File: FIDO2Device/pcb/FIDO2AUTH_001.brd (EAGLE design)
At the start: 22.9 x 34.9 mm, 25 parts, among them CN1 TE-1734028, SW1 SKRPACE010, SW2 SKTADAE010, U1 MDBT50Q-P1M, X1 NX3215SA-32.768K

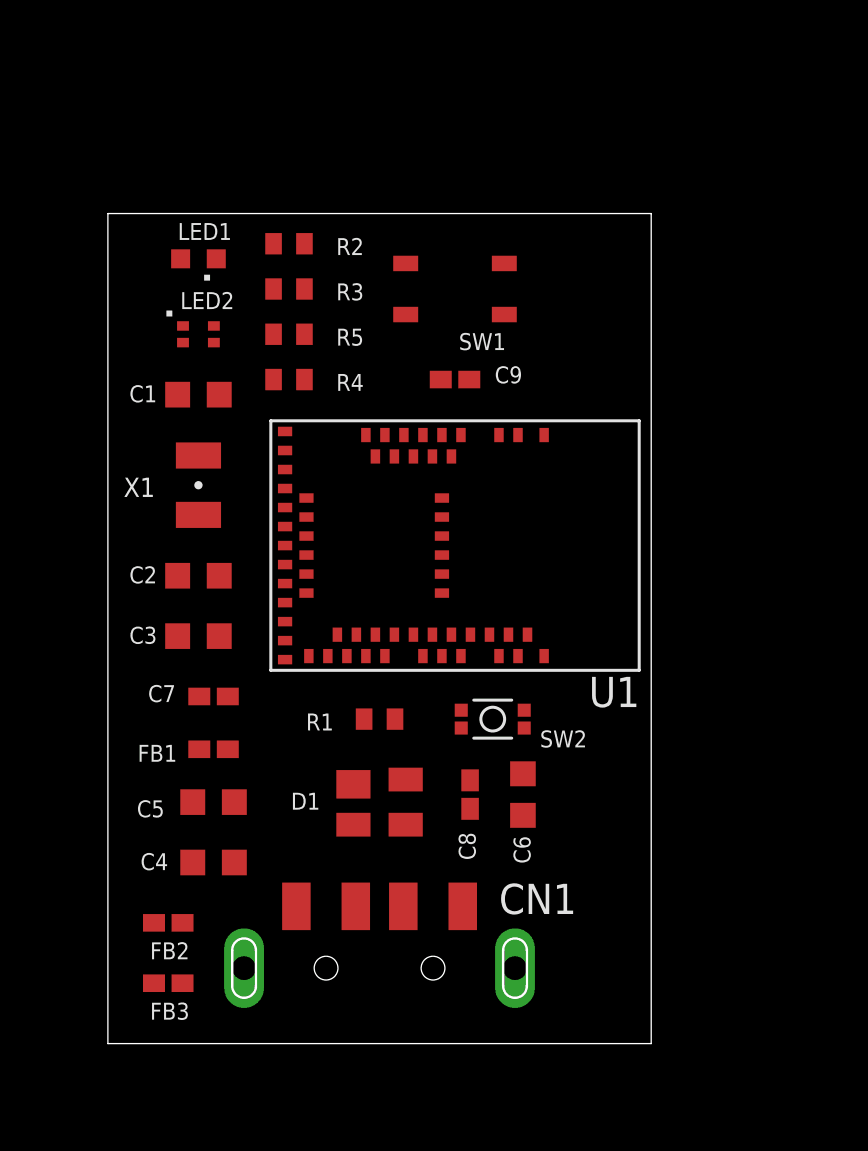
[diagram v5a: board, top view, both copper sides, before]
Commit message: [WIP] ブレークアウト基板回路図
・プログラミング・インターフェース（5Pスルーホール）配置
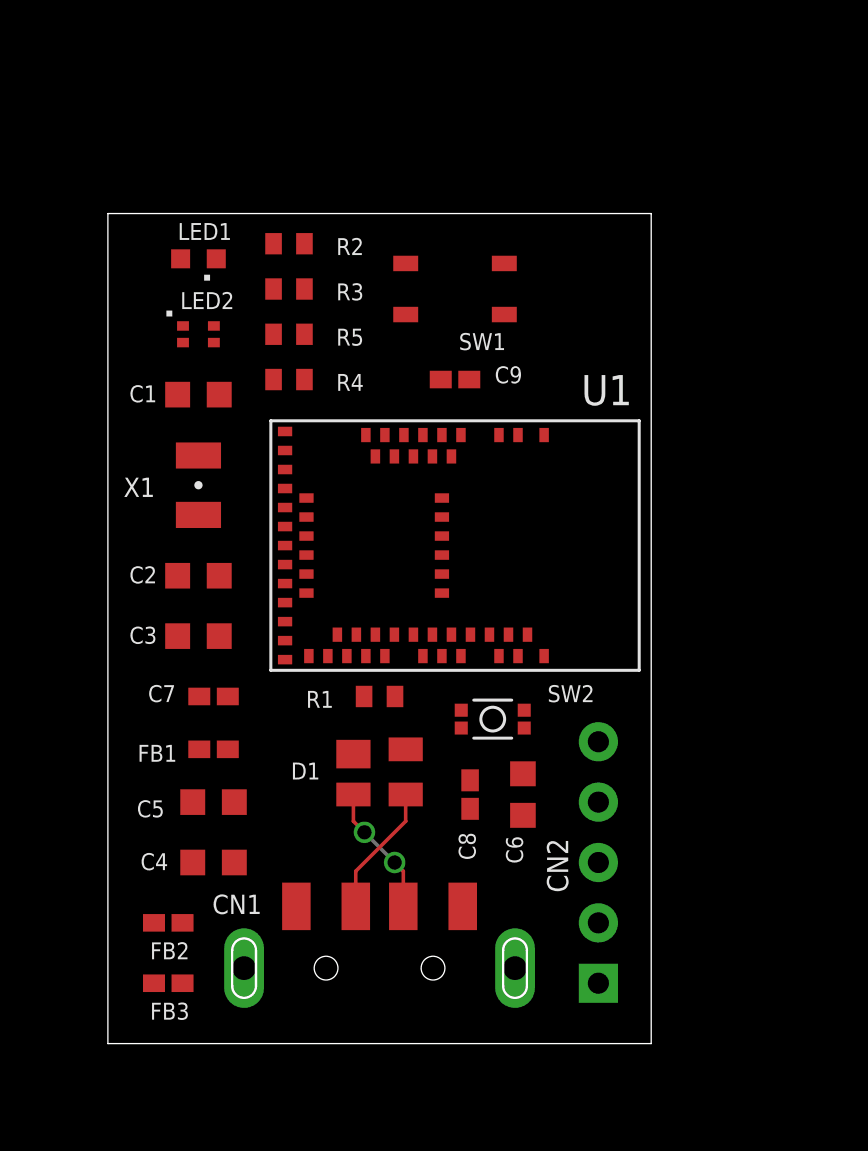
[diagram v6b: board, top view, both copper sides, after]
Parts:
- added CN2: IF_5PIN_H, Connectors:HEADER_5PIN
- moved D1 1.27 mm to (11.4, 11.4)
- moved R1 0.95 mm to (11.4, 14.6)
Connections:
- net 0V: now also CN2.1
- net RESET: now also CN2.5
- net SWDCLK: now also CN2.3
- net SWDIO: now also CN2.2
- net VDD_NRF: now also CN2.4
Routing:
- net D_P: track 0.00 -> 5.57 mm
- net D_N: track 0.00 -> 5.57 mm, vias 0 -> 2
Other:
- board text added: "GND"
- board text added: "PCLK"
- board text added: "PIO"
- board text added: "RST"
- board text added: "VDD"
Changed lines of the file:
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@@
 <wire x1="22.86" y1="34.925" x2="0" y2="34.925" width="0" layer="20"/>
 <wire x1="0" y1="34.925" x2="0" y2="0" width="0" layer="20"/>
+<text x="21.9075" y="2.54" size="0.6096" layer="22" rot="R90" align="top-center">GND</text>
+<text x="21.9075" y="10.16" size="0.6096" layer="22" rot="R90" align="top-center">VDD</text>
+<text x="21.9075" y="12.7" size="0.6096" layer="22" rot="R90" align="top-center">RST</text>
+<text x="21.9075" y="7.62" size="0.6096" layer="22" rot="R90" align="top-center">PCLK</text>
+<text x="21.9075" y="5.08" size="0.6096" layer="22" rot="R90" align="top-center">PIO</text>
 </plain>
 <attributes>
@@
 <elements>
 <element name="U1" library="Parts" package="MDBT50Q-P1M" value="MDBT50Q-P1M" x="14.605" y="20.955" smashed="yes" rot="R270">
-<attribute name="NAME" x="20.235" y="14.16" size="1.27" layer="25"/>
+<attribute name="NAME" x="19.9175" y="26.86" size="1.27" layer="25"/>
 <attribute name="VALUE" x="6.475" y="26.225" size="1.27" layer="27" rot="R270" align="top-left"/>
 </element>
@@
 </element>
 <element name="C6" library="Parts" package="C0603K" value="10uF" x="17.4625" y="10.4775" smashed="yes" rot="R270">
-<attribute name="NAME" x="17.071975" y="8.7376" size="0.7112" layer="25" rot="R270"/>
+<attribute name="NAME" x="16.754475" y="8.7376" size="0.7112" layer="25" rot="R270"/>
 <attribute name="VALUE" x="15.97125" y="11.2775" size="0.7112" layer="27" rot="R270"/>
 </element>
@@
 <attribute name="VALUE" x="3.913125" y="3.99" size="0.7112" layer="27" rot="R180"/>
 </element>
-<element name="D1" library="Parts" package="SOT143B" value="PRTR5V0U2X" x="11.43" y="10.16" smashed="yes" rot="R270">
-<attribute name="NAME" x="7.699375" y="9.8425" size="0.7112" layer="25"/>
-<attribute name="VALUE" x="8.41375" y="11.58875" size="0.7112" layer="27" rot="R270"/>
+<element name="D1" library="Parts" package="SOT143B" value="PRTR5V0U2X" x="11.43" y="11.43" smashed="yes" rot="R270">
+<attribute name="NAME" x="7.699375" y="11.1125" size="0.7112" layer="25"/>
+<attribute name="VALUE" x="8.41375" y="12.85875" size="0.7112" layer="27" rot="R270"/>
 </element>
 <element name="CN1" library="Connectors" package="TE-1734028" value="TE-1734028" x="11.43" y="3.175" smashed="yes">
-<attribute name="NAME" x="16.455" y="5.4525" size="1.27" layer="25"/>
+<attribute name="NAME" x="4.39" y="5.4525" size="0.8128" layer="25"/>
 <attribute name="VALUE" x="6.93" y="-1.325" size="1.27" layer="27"/>
 </element>
-<element name="R1" library="Parts" package="R0402" value="10k" x="11.43" y="13.6525" smashed="yes">
-<attribute name="NAME" x="8.334375" y="13.17625" size="0.7112" layer="25"/>
-<attribute name="VALUE" x="10.874375" y="12.22375" size="0.7112" layer="27"/>
+<element name="R1" library="Parts" package="R0402" value="10k" x="11.43" y="14.605" smashed="yes">
+<attribute name="NAME" x="8.334375" y="14.12875" size="0.7112" layer="25"/>
+<attribute name="VALUE" x="10.874375" y="13.17625" size="0.7112" layer="27"/>
 </element>
 <element name="C9" library="Parts" package="C0402K" value="0.1uF" x="14.605" y="27.94" smashed="yes">
@@
 <element name="SW1" library="Parts" package="SKRPACE010" value="SKRPACE010" x="14.605" y="31.75" rot="R180"/>
 <element name="SW2" library="Parts" package="SKTADAE010" value="SKTADAE010" x="16.1925" y="13.6525" smashed="yes" rot="R180">
-<attribute name="NAME" x="18.176875" y="12.461875" size="0.7112" layer="25" ratio="11"/>
+<attribute name="NAME" x="18.494375" y="14.366875" size="0.7112" layer="25" ratio="11"/>
 <attribute name="VALUE" x="17.541875" y="14.938375" size="0.7112" layer="27" ratio="11" rot="R180" align="top-left"/>
 </element>
@@
 <attribute name="NAME" x="9.604375" y="29.36875" size="0.7112" layer="25"/>
 <attribute name="VALUE" x="7.064375" y="28.41625" size="0.7112" layer="27"/>
+</element>
+<element name="CN2" library="Connectors" package="HEADER_5PIN" value="IF_5PIN_H" x="20.6375" y="2.54" smashed="yes" rot="R90">
+<attribute name="NAME" x="19.3675" y="6.35" size="0.889" layer="25" ratio="11" rot="R90"/>
+<attribute name="VALUE" x="21.9075" y="1.27" size="0.889" layer="27" ratio="11" rot="R90" align="top-left"/>
 </element>
 </elements>
@@
 <contactref element="SW2" pad="3"/>
 <contactref element="SW2" pad="1"/>
+<contactref element="CN2" pad="1"/>
 <wire x1="12.53" y1="32.825" x2="16.68" y2="32.825" width="0" layer="19" extent="1-1"/>
-<wire x1="15.205" y1="27.94" x2="12.53" y2="32.825" width="0" layer="19" extent="1-1"/>
+<wire x1="15.205" y1="27.94" x2="16.68" y2="32.825" width="0" layer="19" extent="1-1"/>
 <wire x1="17.255" y1="25.605" x2="15.205" y2="27.94" width="0" layer="19" extent="1-1"/>
 <wire x1="18.355" y1="25.605" x2="17.255" y2="25.605" width="0" layer="19" extent="1-1"/>
@@
 <wire x1="1.94" y1="5.08" x2="3.57" y2="7.62" width="0" layer="19" extent="1-1"/>
 <wire x1="1.94" y1="2.54" x2="1.94" y2="5.08" width="0" layer="19" extent="1-1"/>
-<wire x1="10.33" y1="10.91" x2="7.455" y2="16.155" width="0" layer="19" extent="1-1"/>
-<wire x1="15.24" y1="9.8775" x2="10.33" y2="10.91" width="0" layer="19" extent="1-1"/>
+<wire x1="10.33" y1="12.18" x2="7.455" y2="16.155" width="0" layer="19" extent="1-1"/>
+<wire x1="15.24" y1="9.8775" x2="10.33" y2="12.18" width="0" layer="19" extent="1-1"/>
 <wire x1="17.4625" y1="9.6025" x2="15.24" y2="9.8775" width="0" layer="19" extent="1-1"/>
 <wire x1="17.5175" y1="13.2775" x2="17.4625" y2="9.6025" width="0" layer="19" extent="1-1"/>
 <wire x1="17.5175" y1="14.0275" x2="17.5175" y2="13.2775" width="0" layer="19" extent="1-1"/>
 <wire x1="18.355" y1="16.305" x2="17.5175" y2="14.0275" width="0" layer="19" extent="1-1"/>
+<wire x1="20.6375" y1="2.54" x2="17.4625" y2="9.6025" width="0" layer="19" extent="1-1"/>
 </signal>
 <signal name="XL1">
@@
 <signal name="SWDCLK">
 <contactref element="U1" pad="53"/>
+<contactref element="CN2" pad="3"/>
+<wire x1="20.6375" y1="7.62" x2="17.255" y2="16.305" width="0" layer="19" extent="1-1"/>
 </signal>
 <signal name="SWDIO">
 <contactref element="U1" pad="51"/>
+<contactref element="CN2" pad="2"/>
+<wire x1="20.6375" y1="5.08" x2="16.455" y2="16.305" width="0" layer="19" extent="1-1"/>
 </signal>
 <signal name="RESET">
@@
 <contactref element="SW2" pad="2"/>
 <contactref element="SW2" pad="4"/>
+<contactref element="CN2" pad="5"/>
 <wire x1="11.255" y1="17.205" x2="14.005" y2="27.94" width="0" layer="19" extent="1-1"/>
-<wire x1="12.08" y1="13.6525" x2="11.255" y2="17.205" width="0" layer="19" extent="1-1"/>
-<wire x1="14.8675" y1="13.2775" x2="12.08" y2="13.6525" width="0" layer="19" extent="1-1"/>
-<wire x1="14.8675" y1="14.0275" x2="14.8675" y2="13.2775" width="0" layer="19" extent="1-1"/>
+<wire x1="12.08" y1="14.605" x2="11.255" y2="17.205" width="0" layer="19" extent="1-1"/>
+<wire x1="14.8675" y1="14.0275" x2="12.08" y2="14.605" width="0" layer="19" extent="1-1"/>
+<wire x1="14.8675" y1="13.2775" x2="14.8675" y2="14.0275" width="0" layer="19" extent="1-1"/>
+<wire x1="20.6375" y1="12.7" x2="14.8675" y2="13.2775" width="0" layer="19" extent="1-1"/>
 </signal>
 <signal name="D_P">
@@
 <contactref element="D1" pad="3"/>
 <contactref element="CN1" pad="3"/>
-<wire x1="12.53" y1="9.21" x2="9.255" y2="16.305" width="0" layer="19" extent="1-1"/>
-<wire x1="10.43" y1="5.775" x2="12.53" y2="9.21" width="0" layer="19" extent="1-1"/>
+<wire x1="10.43" y1="5.775" x2="10.43" y2="7.255" width="0.1524" layer="1"/>
+<wire x1="12.53" y1="10.48" x2="12.53" y2="9.355" width="0.1524" layer="1"/>
+<wire x1="12.53" y1="9.355" x2="10.43" y2="7.255" width="0.1524" layer="1"/>
+<wire x1="12.53" y1="10.48" x2="9.255" y2="16.305" width="0" layer="19" extent="1-1"/>
 </signal>
 <signal name="D_N">
@@
 <contactref element="D1" pad="2"/>
 <contactref element="CN1" pad="2"/>
-<wire x1="10.33" y1="9.21" x2="8.455" y2="16.305" width="0" layer="19" extent="1-1"/>
-<wire x1="12.43" y1="5.775" x2="10.33" y2="9.21" width="0" layer="19" extent="1-1"/>
+<via x="10.795" y="8.89" extent="1-16" drill="0.6"/>
+<via x="12.065" y="7.62" extent="1-16" drill="0.6"/>
+<wire x1="12.43" y1="5.775" x2="12.43" y2="7.255" width="0.1524" layer="1"/>
+<wire x1="12.43" y1="7.255" x2="12.065" y2="7.62" width="0.1524" layer="1"/>
+<wire x1="10.795" y1="8.89" x2="10.33" y2="9.355" width="0.1524" layer="1"/>
+<wire x1="10.33" y1="9.355" x2="10.33" y2="10.48" width="0.1524" layer="1"/>
+<wire x1="10.795" y1="8.89" x2="12.065" y2="7.62" width="0.1524" layer="16"/>
+<wire x1="10.33" y1="10.48" x2="8.455" y2="16.305" width="0" layer="19" extent="1-1"/>
 </signal>
 <signal name="VDD_NRF">
@@
 <contactref element="LED1" pad="A"/>
 <contactref element="LED2" pad="1"/>
+<contactref element="CN2" pad="4"/>
 <wire x1="3.16" y1="30.195" x2="3.06" y2="33.02" width="0" layer="19" extent="1-1"/>
 <wire x1="7.455" y1="19.355" x2="3.16" y2="30.195" width="0" layer="19" extent="1-1"/>
 <wire x1="7.455" y1="18.555" x2="7.455" y2="19.355" width="0" layer="19" extent="1-1"/>
 <wire x1="4.685" y1="17.145" x2="7.455" y2="18.555" width="0" layer="19" extent="1-1"/>
-<wire x1="10.78" y1="13.6525" x2="7.455" y2="18.555" width="0" layer="19" extent="1-1"/>
+<wire x1="10.78" y1="14.605" x2="7.455" y2="18.555" width="0" layer="19" extent="1-1"/>
+<wire x1="20.6375" y1="10.16" x2="10.78" y2="14.605" width="0" layer="19" extent="1-1"/>
 </signal>
 <signal name="VBUS">
@@
 <contactref element="D1" pad="4"/>
 <wire x1="17.4625" y1="11.3525" x2="15.24" y2="11.0775" width="0" layer="19" extent="1-1"/>
-<wire x1="12.53" y1="11.11" x2="15.24" y2="11.0775" width="0" layer="19" extent="1-1"/>
+<wire x1="12.53" y1="12.38" x2="15.24" y2="11.0775" width="0" layer="19" extent="1-1"/>
 <wire x1="14.93" y1="5.775" x2="15.24" y2="11.0775" width="0" layer="19" extent="1-1"/>
-<wire x1="5.32" y1="10.16" x2="12.53" y2="11.11" width="0" layer="19" extent="1-1"/>
+<wire x1="5.32" y1="10.16" x2="12.53" y2="12.38" width="0" layer="19" extent="1-1"/>
 <wire x1="3.845" y1="12.3825" x2="5.32" y2="10.16" width="0" layer="19" extent="1-1"/>
 </signal>

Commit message: [WIP] ブレークアウト基板回路図
・電源供給回路を追加
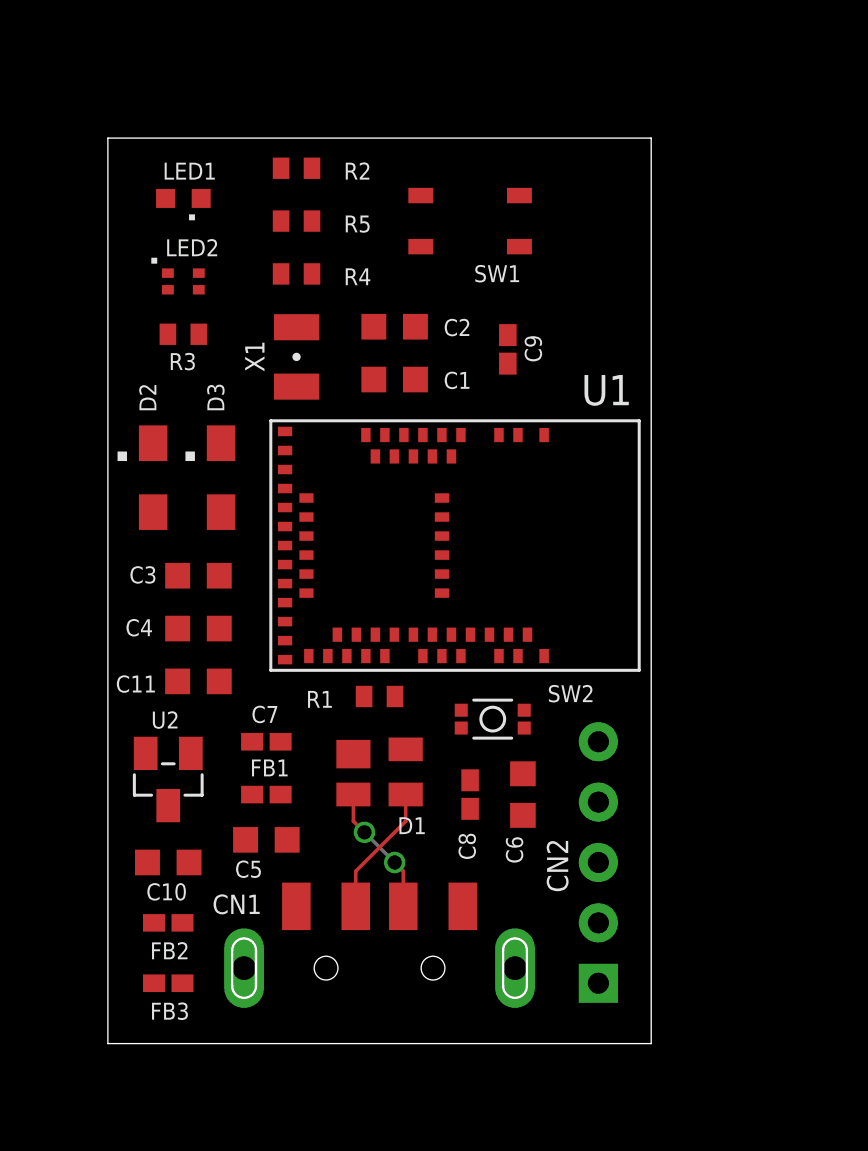
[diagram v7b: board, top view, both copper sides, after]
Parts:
- added C10, C11: 1uF, Parts:C0603K
- added D2, D3: PMEG2005AEA,115, Parts:SOD323-W
- added U2: XC6206P332MR-G, Parts:SOT23
- C5: value 10uF -> 0.01uF
- moved C2 13.3 mm to (12.1, 30.2), turned to 0 degrees
- moved C4 9.86 mm to (3.81, 17.5)
- moved C1 8.28 mm to (12.1, 27.9), turned to 0 degrees
- moved X1 6.79 mm to (7.94, 28.9), turned to 90 degrees
- moved R3 4.84 mm to (3.17, 29.8), turned to 180 degrees
- moved R5 4.77 mm to (7.94, 34.6)
- moved R4 4.46 mm to (7.94, 32.4)
- moved R2 3.19 mm to (7.94, 36.8)
- moved SW1 2.93 mm to (15.2, 34.6)
- moved C7 2.93 mm to (6.67, 12.7), turned to 0 degrees
- moved FB1 2.93 mm to (6.67, 10.5), turned to 180 degrees
- moved C5 2.73 mm to (6.67, 8.57)
- moved LED1 2.62 mm to (3.17, 35.6)
- moved C9 2.56 mm to (16.8, 29.2), turned to 90 degrees
- moved C3 2.54 mm to (3.81, 19.7)
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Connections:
- new net N$4: C11.1, D2.A, U2.2
- net 0V: now also C10.2, C11.2, U2.1
- net VBUS_NRF: now also C10.1, U2.3
- net VDD_NRF: now also D2.C, D3.C
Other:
- board size 22.9 x 34.9 mm -> 22.9 x 38.1 mm

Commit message: [WIP] ブレークアウト基板回路図
・電池ホルダー（CR1225用、3.0V）を追加
・汎用I/O用のヘッダーピン（3Pin）を追加
・プリント基板上の配線作業を開始
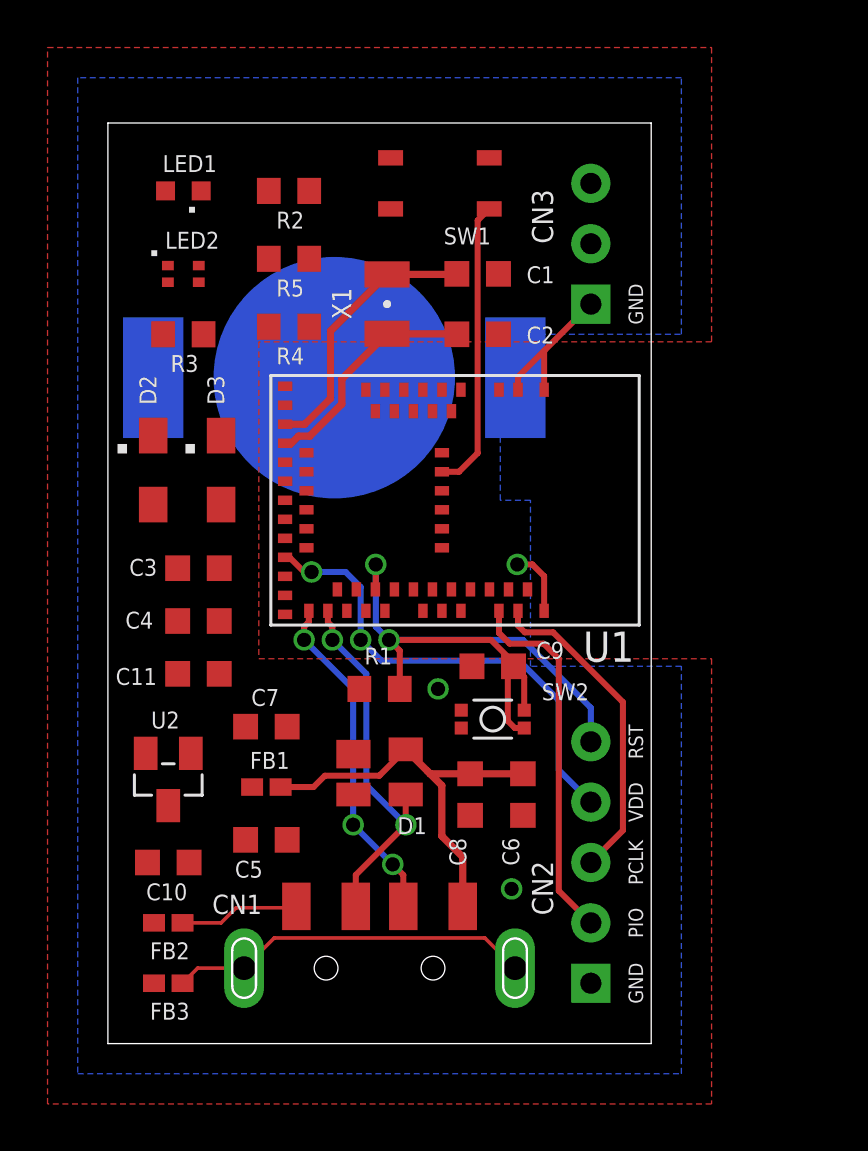
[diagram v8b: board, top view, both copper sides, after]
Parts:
- added BAT1: BAT-HLD-012-SMT, Connectors:BAT-HLD-012-SMT
- added CN3: IF_3PIN, Connectors:HEADER_3PIN
- C7, C8, C9: device Parts:C0402K -> Parts:C0603K
- R1, R2, R3, R4, R5: device Parts:R0402 -> Parts:R0603
- moved C9 13.4 mm to (16.2, 15.9), turned to 180 degrees
- moved C1 5.65 mm to (15.6, 32.4)
- moved X1 4.41 mm to (11.7, 31.1), turned to 270 degrees
- moved C2 3.51 mm to (15.6, 29.8)
- moved R4 2.25 mm to (7.62, 30.2), turned to 180 degrees
- moved SW1 2.03 mm to (14.0, 36.2)
- moved U1 1.91 mm to (14.6, 22.9)
- moved R5 1.62 mm to (7.62, 33.0), turned to 180 degrees
- moved R2 1.00 mm to (7.62, 35.9), turned to 180 degrees
- moved C7 0.64 mm to (6.67, 13.3)
- moved C3 0.32 mm to (3.81, 20.0)
- moved C4 0.32 mm to (3.81, 17.8)
- moved FB1 0.32 mm to (6.67, 10.8)
- moved C11 0.32 mm to (3.81, 15.6)
- moved CN2 0.32 mm to (20.3, 2.54)
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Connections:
- new net N$5: BAT1.+@1, BAT1.+@2, D3.A
- net 0V: now also BAT1.-, CN3.1
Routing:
- net RESET: track 0.00 -> 28.9 mm, vias 0 -> 2
- net VDD_NRF: track 0.00 -> 20.2 mm, vias 0 -> 2
- net VBUS: track 0.00 -> 17.4 mm
- net SWDIO: track 0.00 -> 15.6 mm
- net N$3: track 0.00 -> 15.3 mm
- net SWDCLK: track 0.00 -> 13.7 mm
- net SW1: track 0.00 -> 12.3 mm
- net XL1: track 0.00 -> 11.5 mm
- net D_P: track 5.57 -> 15.9 mm, vias 0 -> 2
- net XL2: track 0.00 -> 9.76 mm
- net 0V: track 0.00 -> 9.31 mm, vias 0 -> 3
- net D_N: track 5.57 -> 14.2 mm, vias 2 -> 3
- net N$2: track 0.00 -> 5.08 mm
- added copper zone on layer 1, net 0V
- added copper zone on layer 16, net 0V
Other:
- board size 22.9 x 38.1 mm -> 22.9 x 38.7 mm
